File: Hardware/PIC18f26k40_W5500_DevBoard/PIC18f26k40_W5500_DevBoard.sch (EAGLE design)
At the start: 39 parts, among them J2 MAGJACK, U1 W5500, U2 PIC18F2523-I/SO

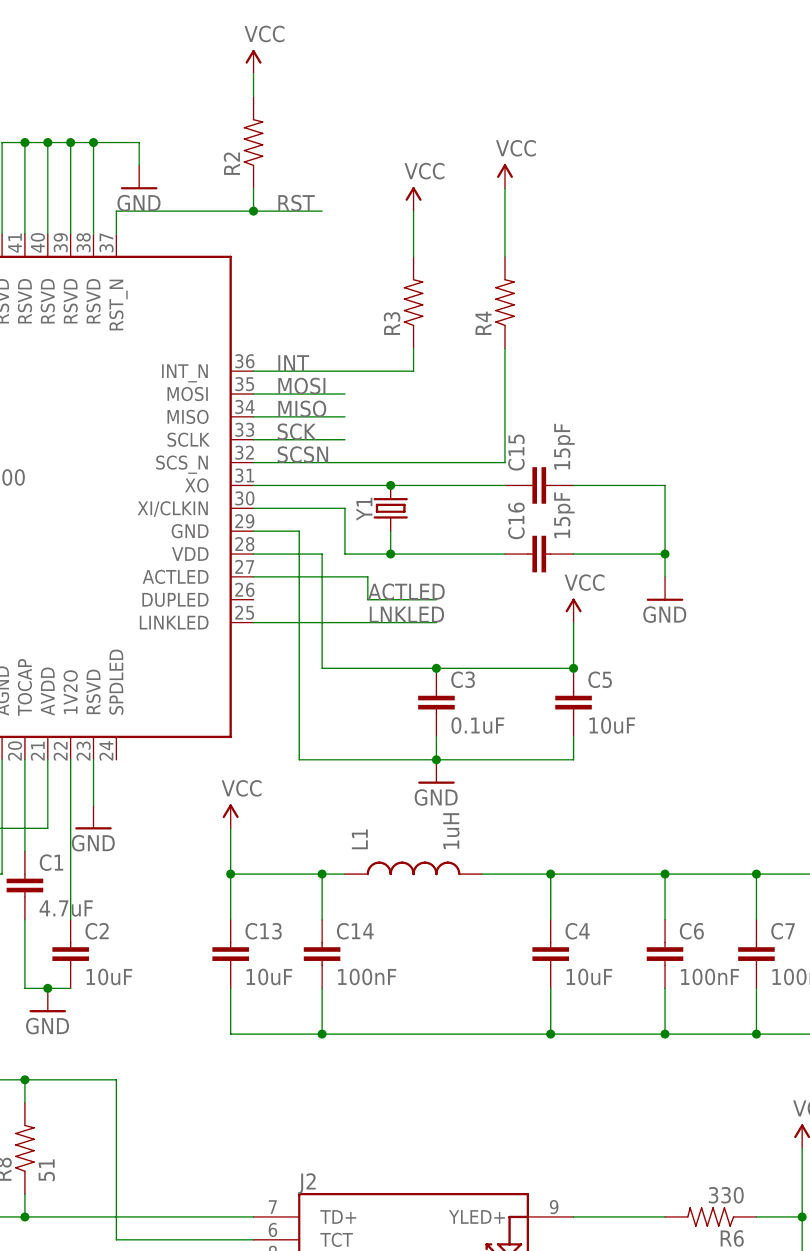
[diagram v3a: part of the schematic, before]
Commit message: #251 Arranged components on board
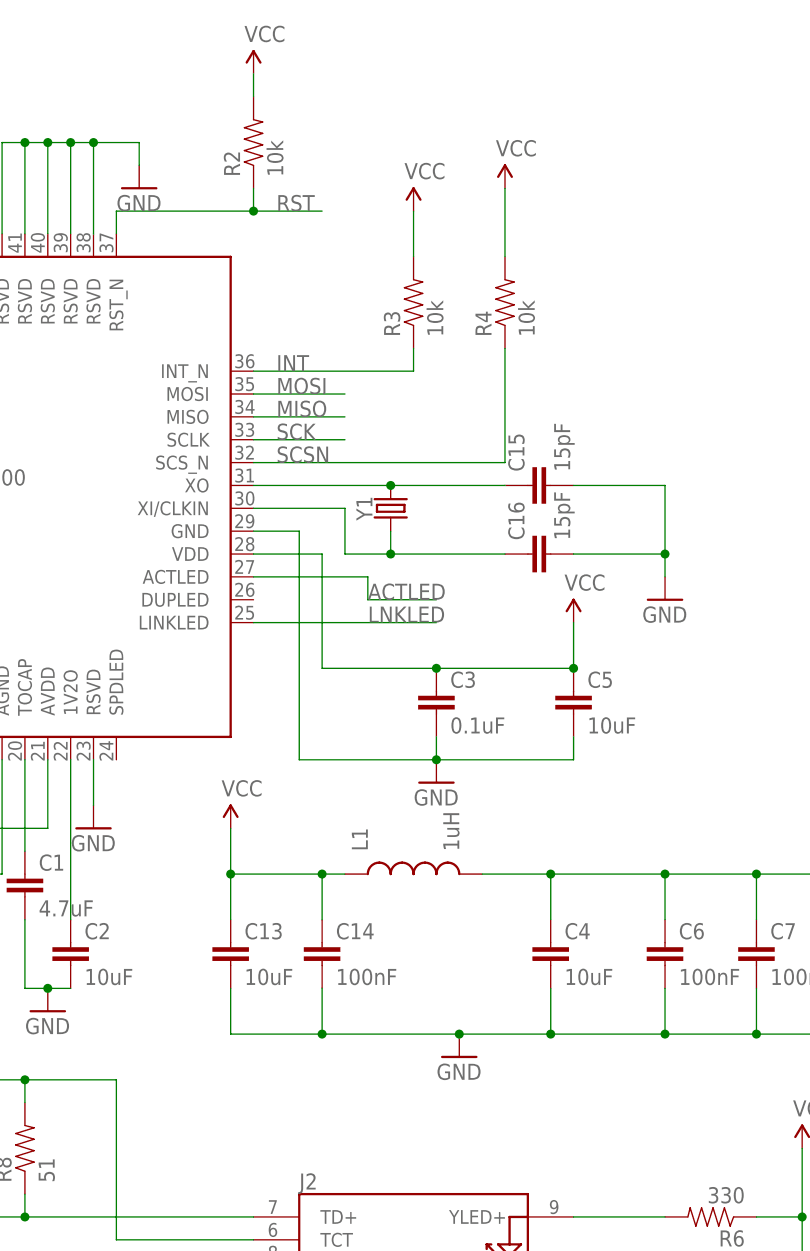
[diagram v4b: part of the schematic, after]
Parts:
- R2, R3, R4: value (none) -> 10k
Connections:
- removed net N$3: C10.2, C11.2, C12.2, C13.2, C14.2, C4.2, C6.2, C7.2, C8.2, C9.2
- net GND: now also C10.2, C11.2, C12.2, C13.2, C14.2, C4.2, C6.2, C7.2, C8.2, C9.2
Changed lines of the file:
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@@
 <part name="C5" library="SparkFun-Passives" deviceset="CAP" device="0603-CAP" value="10uF"/>
 <part name="GND4" library="SparkFun-Aesthetics" deviceset="GND" device=""/>
-<part name="R2" library="SparkFun-Passives" deviceset="RESISTOR" device="0603-RES"/>
-<part name="R3" library="SparkFun-Passives" deviceset="RESISTOR" device="0603-RES"/>
+<part name="R2" library="SparkFun-Passives" deviceset="RESISTOR" device="0603-RES" value="10k"/>
+<part name="R3" library="SparkFun-Passives" deviceset="RESISTOR" device="0603-RES" value="10k"/>
 <part name="SUPPLY2" library="SparkFun-Aesthetics" deviceset="VCC" device=""/>
 <part name="SUPPLY3" library="SparkFun-Aesthetics" deviceset="VCC" device=""/>
@@
 <part name="C14" library="SparkFun-Passives" deviceset="CAP" device="0603-CAP" value="100nF"/>
 <part name="SUPPLY5" library="SparkFun-Aesthetics" deviceset="VCC" device=""/>
-<part name="R4" library="SparkFun-Passives" deviceset="RESISTOR" device="0603-RES"/>
+<part name="R4" library="SparkFun-Passives" deviceset="RESISTOR" device="0603-RES" value="10k"/>
 <part name="SUPPLY6" library="SparkFun-Aesthetics" deviceset="VCC" device=""/>
 <part name="GND5" library="SparkFun-Aesthetics" deviceset="GND" device=""/>
@@
 <part name="GND16" library="SparkFun-Aesthetics" deviceset="GND" device=""/>
 <part name="SUPPLY11" library="SparkFun-Aesthetics" deviceset="VCC" device=""/>
+<part name="GND17" library="SparkFun-Aesthetics" deviceset="GND" device=""/>
 </parts>
 <sheets>
@@
 <instance part="GND16" gate="1" x="81.28" y="-30.48"/>
 <instance part="SUPPLY11" gate="G$1" x="81.28" y="-17.78"/>
+<instance part="GND17" gate="1" x="259.08" y="25.4"/>
 </instances>
 <busses>
@@
 <pinref part="GND16" gate="1" pin="GND"/>
 </segment>
-</net>
-<net name="N$1" class="0">
-<segment>
-<pinref part="U1" gate="G$1" pin="TOCAP"/>
-<pinref part="C1" gate="G$1" pin="1"/>
-<wire x1="210.82" y1="58.42" x2="210.82" y2="48.26" width="0.1524" layer="91"/>
-</segment>
-</net>
-<net name="N$2" class="0">
-<segment>
-<pinref part="U1" gate="G$1" pin="1V2O"/>
-<pinref part="C2" gate="G$1" pin="1"/>
-<wire x1="215.9" y1="58.42" x2="215.9" y2="40.64" width="0.1524" layer="91"/>
-</segment>
-</net>
-<net name="N$4" class="0">
-<segment>
-<pinref part="U1" gate="G$1" pin="EXRES1"/>
-<pinref part="R1" gate="G$1" pin="2"/>
-<wire x1="177.8" y1="78.74" x2="162.56" y2="78.74" width="0.1524" layer="91"/>
-<wire x1="162.56" y1="78.74" x2="162.56" y2="68.58" width="0.1524" layer="91"/>
-</segment>
-</net>
-<net name="INT" class="0">
-<segment>
-<pinref part="U1" gate="G$1" pin="INT_N"/>
-<wire x1="236.22" y1="101.6" x2="254" y2="101.6" width="0.1524" layer="91"/>
-<label x="238.76" y="101.6" size="1.778" layer="95"/>
-<pinref part="R3" gate="G$1" pin="1"/>
-<wire x1="254" y1="101.6" x2="254" y2="104.14" width="0.1524" layer="91"/>
-</segment>
-</net>
-<net name="RST" class="0">
-<segment>
-<pinref part="U1" gate="G$1" pin="RST_N"/>
-<wire x1="220.98" y1="116.84" x2="220.98" y2="119.38" width="0.1524" layer="91"/>
-<wire x1="220.98" y1="119.38" x2="236.22" y2="119.38" width="0.1524" layer="91"/>
-<label x="238.76" y="119.38" size="1.778" layer="95"/>
-<pinref part="R2" gate="G$1" pin="1"/>
-<wire x1="236.22" y1="119.38" x2="243.84" y2="119.38" width="0.1524" layer="91"/>
-<wire x1="236.22" y1="121.92" x2="236.22" y2="119.38" width="0.1524" layer="91"/>
-<junction x="236.22" y="119.38"/>
-</segment>
-</net>
-<net name="N$3" class="0">
 <segment>
 <pinref part="C4" gate="G$1" pin="2"/>
@@
 <junction x="269.24" y="27.94"/>
 <pinref part="C14" gate="G$1" pin="2"/>
-<wire x1="243.84" y1="27.94" x2="269.24" y2="27.94" width="0.1524" layer="91"/>
+<wire x1="243.84" y1="27.94" x2="259.08" y2="27.94" width="0.1524" layer="91"/>
+<wire x1="259.08" y1="27.94" x2="269.24" y2="27.94" width="0.1524" layer="91"/>
 <wire x1="243.84" y1="33.02" x2="243.84" y2="27.94" width="0.1524" layer="91"/>
 <junction x="243.84" y="27.94"/>
-</segment>
-</net>
+<pinref part="GND17" gate="1" pin="GND"/>
+<junction x="259.08" y="27.94"/>
+</segment>
+</net>
+<net name="N$1" class="0">
+<segment>
+<pinref part="U1" gate="G$1" pin="TOCAP"/>
+<pinref part="C1" gate="G$1" pin="1"/>
+<wire x1="210.82" y1="58.42" x2="210.82" y2="48.26" width="0.1524" layer="91"/>
+</segment>
+</net>
+<net name="N$2" class="0">
+<segment>
+<pinref part="U1" gate="G$1" pin="1V2O"/>
+<pinref part="C2" gate="G$1" pin="1"/>
+<wire x1="215.9" y1="58.42" x2="215.9" y2="40.64" width="0.1524" layer="91"/>
+</segment>
+</net>
+<net name="N$4" class="0">
+<segment>
+<pinref part="U1" gate="G$1" pin="EXRES1"/>
+<pinref part="R1" gate="G$1" pin="2"/>
+<wire x1="177.8" y1="78.74" x2="162.56" y2="78.74" width="0.1524" layer="91"/>
+<wire x1="162.56" y1="78.74" x2="162.56" y2="68.58" width="0.1524" layer="91"/>
+</segment>
+</net>
+<net name="INT" class="0">
+<segment>
+<pinref part="U1" gate="G$1" pin="INT_N"/>
+<wire x1="236.22" y1="101.6" x2="254" y2="101.6" width="0.1524" layer="91"/>
+<label x="238.76" y="101.6" size="1.778" layer="95"/>
+<pinref part="R3" gate="G$1" pin="1"/>
+<wire x1="254" y1="101.6" x2="254" y2="104.14" width="0.1524" layer="91"/>
+</segment>
+</net>
+<net name="RST" class="0">
+<segment>
+<pinref part="U1" gate="G$1" pin="RST_N"/>
+<wire x1="220.98" y1="116.84" x2="220.98" y2="119.38" width="0.1524" layer="91"/>
+<wire x1="220.98" y1="119.38" x2="236.22" y2="119.38" width="0.1524" layer="91"/>
+<label x="238.76" y="119.38" size="1.778" layer="95"/>
+<pinref part="R2" gate="G$1" pin="1"/>
+<wire x1="236.22" y1="119.38" x2="243.84" y2="119.38" width="0.1524" layer="91"/>
+<wire x1="236.22" y1="121.92" x2="236.22" y2="119.38" width="0.1524" layer="91"/>
+<junction x="236.22" y="119.38"/>
+</segment>
+</net>

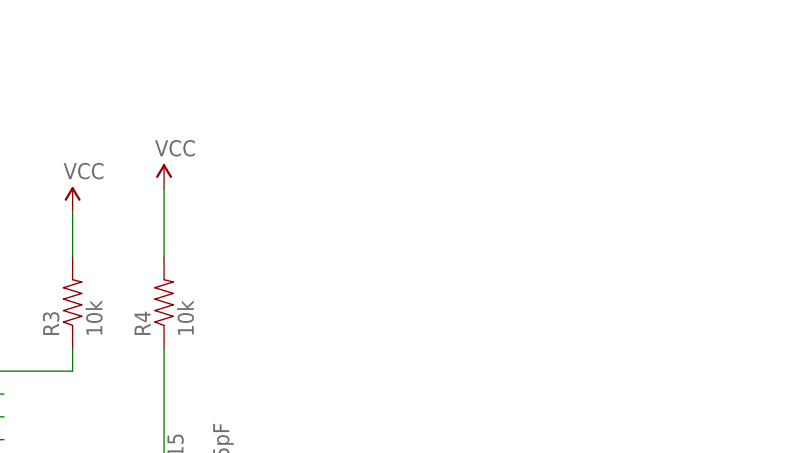
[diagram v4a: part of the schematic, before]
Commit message: #251 Added more labeling to board
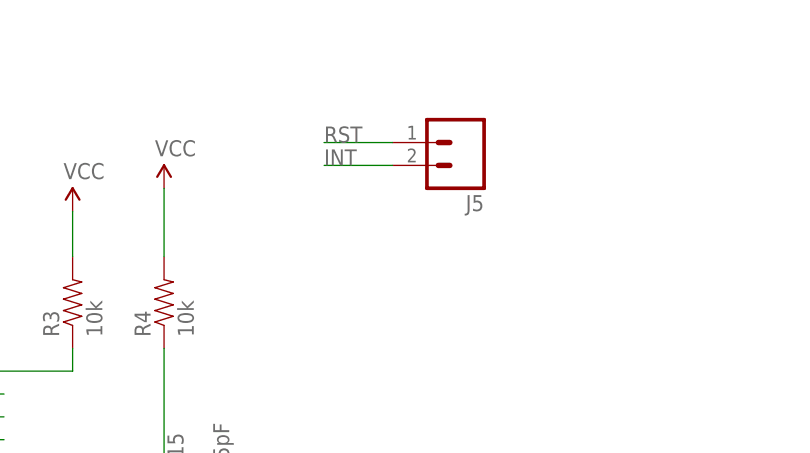
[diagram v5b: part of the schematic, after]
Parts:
- added J5: (no value), SparkFun-Connectors:M02PTH
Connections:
- net INT: now also J5.2
- net RST: now also J5.1
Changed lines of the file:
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@@
 <part name="SUPPLY11" library="SparkFun-Aesthetics" deviceset="VCC" device=""/>
 <part name="GND17" library="SparkFun-Aesthetics" deviceset="GND" device=""/>
+<part name="J5" library="SparkFun-Connectors" deviceset="M02" device="PTH"/>
 </parts>
 <sheets>
@@
 <instance part="SUPPLY11" gate="G$1" x="81.28" y="-17.78"/>
 <instance part="GND17" gate="1" x="259.08" y="25.4"/>
+<instance part="J5" gate="G$1" x="297.18" y="127" rot="R180"/>
 </instances>
 <busses>
@@
 <wire x1="254" y1="101.6" x2="254" y2="104.14" width="0.1524" layer="91"/>
 </segment>
+<segment>
+<pinref part="J5" gate="G$1" pin="2"/>
+<wire x1="289.56" y1="124.46" x2="281.94" y2="124.46" width="0.1524" layer="91"/>
+<label x="281.94" y="124.46" size="1.778" layer="95"/>
+</segment>
 </net>
 <net name="RST" class="0">
@@
 <junction x="236.22" y="119.38"/>
 </segment>
-</net>
+<segment>
+<pinref part="J5" gate="G$1" pin="1"/>
+<wire x1="289.56" y1="127" x2="281.94" y2="127" width="0.1524" layer="91"/>
+<label x="281.94" y="127" size="1.778" layer="95"/>
+</segment>
+</net>

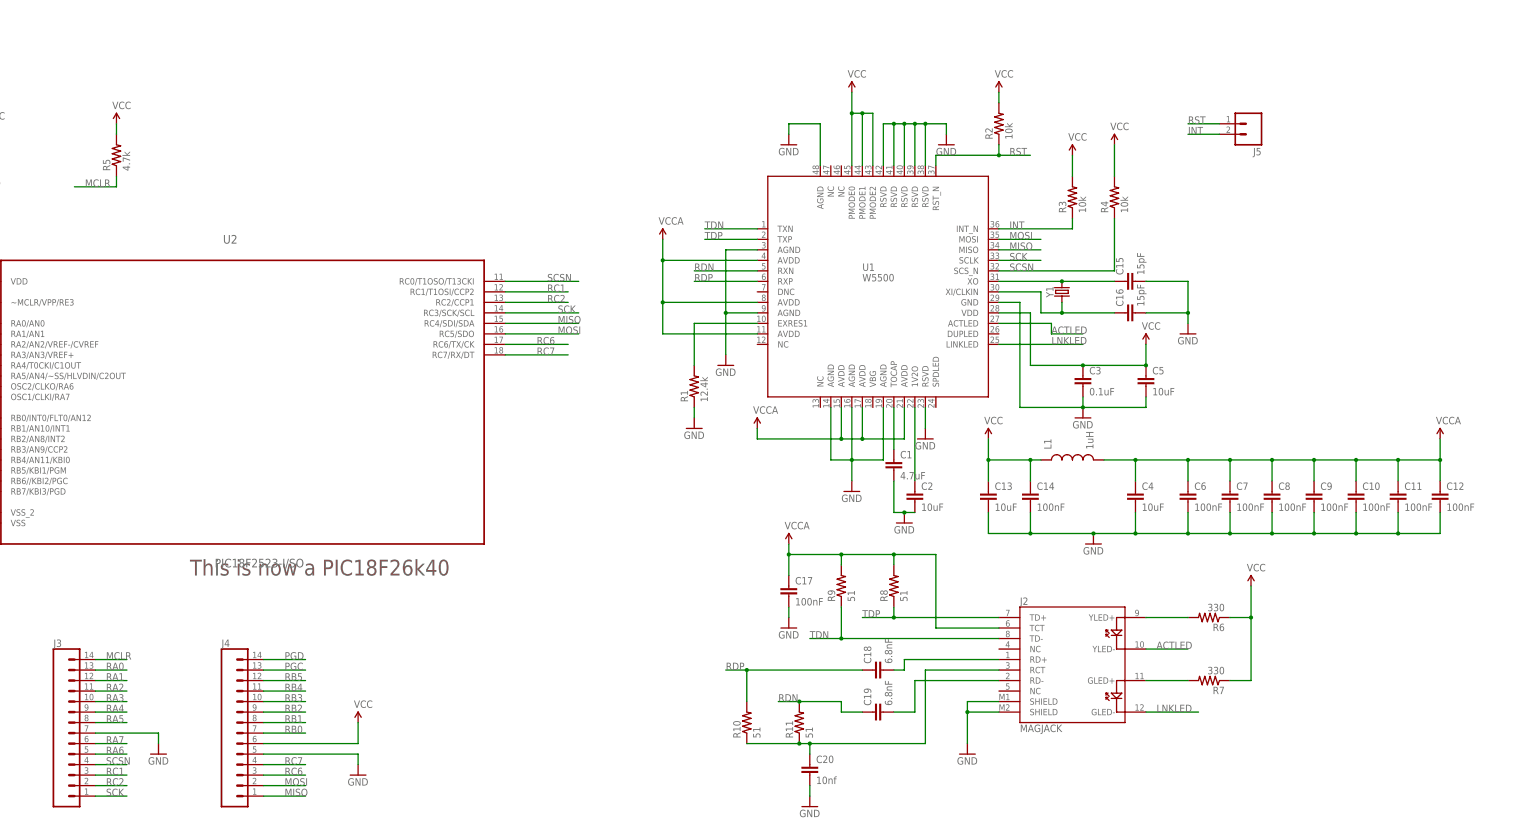
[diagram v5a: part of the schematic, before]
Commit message: #251 Added some labeling to the circuit schematic
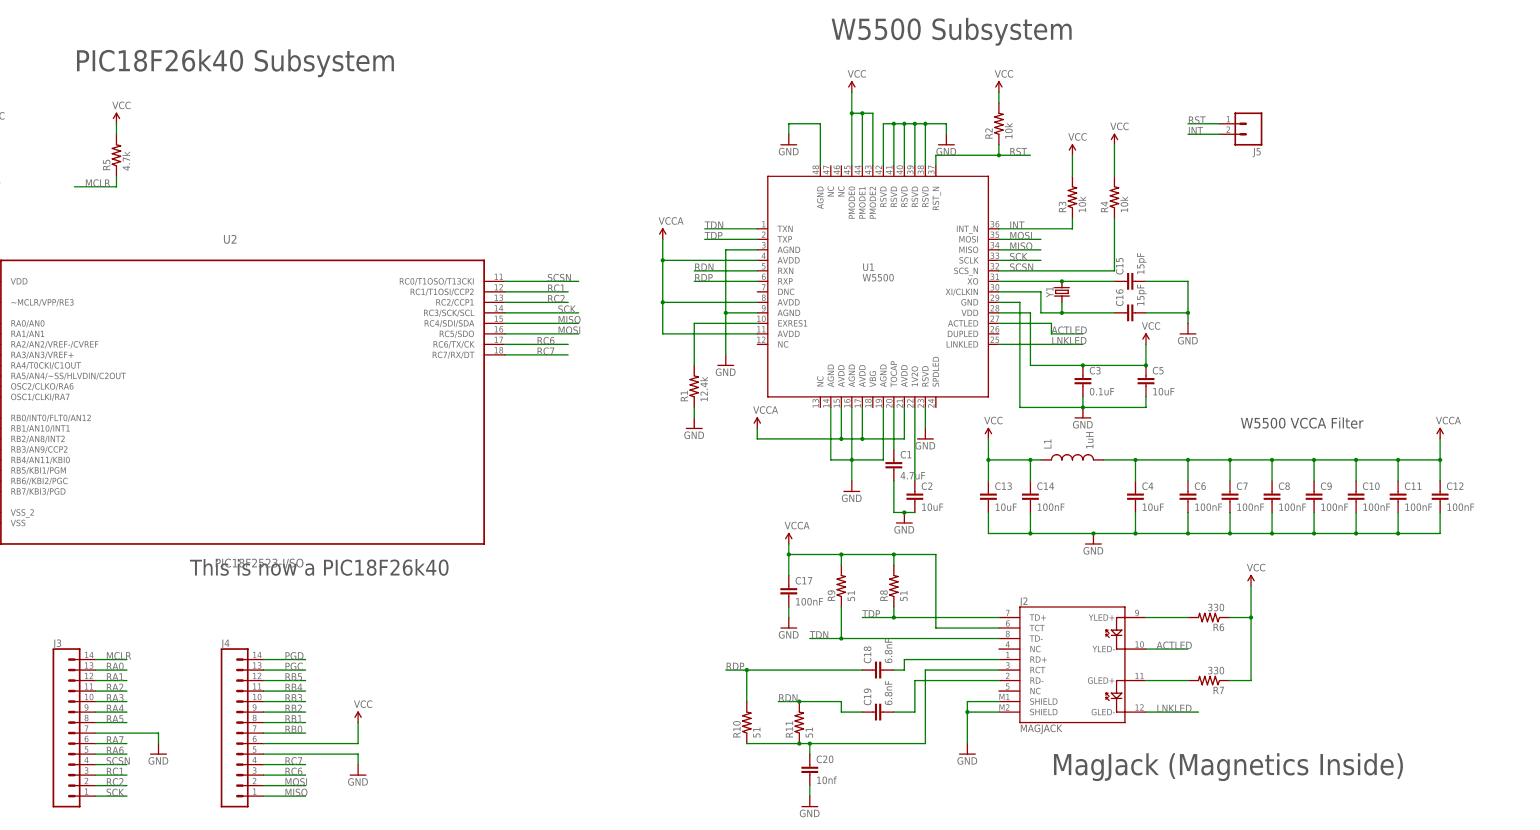
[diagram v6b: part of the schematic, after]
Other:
- note added: "MagJack (Magnetics Inside)"
- note added: "PIC18F26k40 Subsystem"
- note added: "W5500 Subsystem"
- note added: "W5500 VCCA Filter"
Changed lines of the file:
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@@
 <plain>
 <text x="40.64" y="17.78" size="3.81" layer="97">This is now a PIC18F26k40</text>
+<text x="12.7" y="139.7" size="5.08" layer="97">PIC18F26k40 Subsystem</text>
+<text x="195.58" y="147.32" size="5.08" layer="97">W5500 Subsystem</text>
+<text x="294.64" y="53.34" size="2.54" layer="97">W5500 VCCA Filter</text>
+<text x="248.92" y="-30.48" size="5.08" layer="97">MagJack (Magnetics Inside)</text>
 </plain>
 <instances>
